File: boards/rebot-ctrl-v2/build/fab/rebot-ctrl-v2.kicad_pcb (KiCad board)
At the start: 4 copper layers, 25 x 25 mm, 57 parts, among them J1 JST-SH 8P (ESC), J2 JST-GH 4P (receiver), J3 USB-C 16P, U1 STM32G431KBU6, U2 LMR36506 buck, U3 XC6206 3.3V, U4 LSM6DSV32X, U5 W25Q128JV 16MB

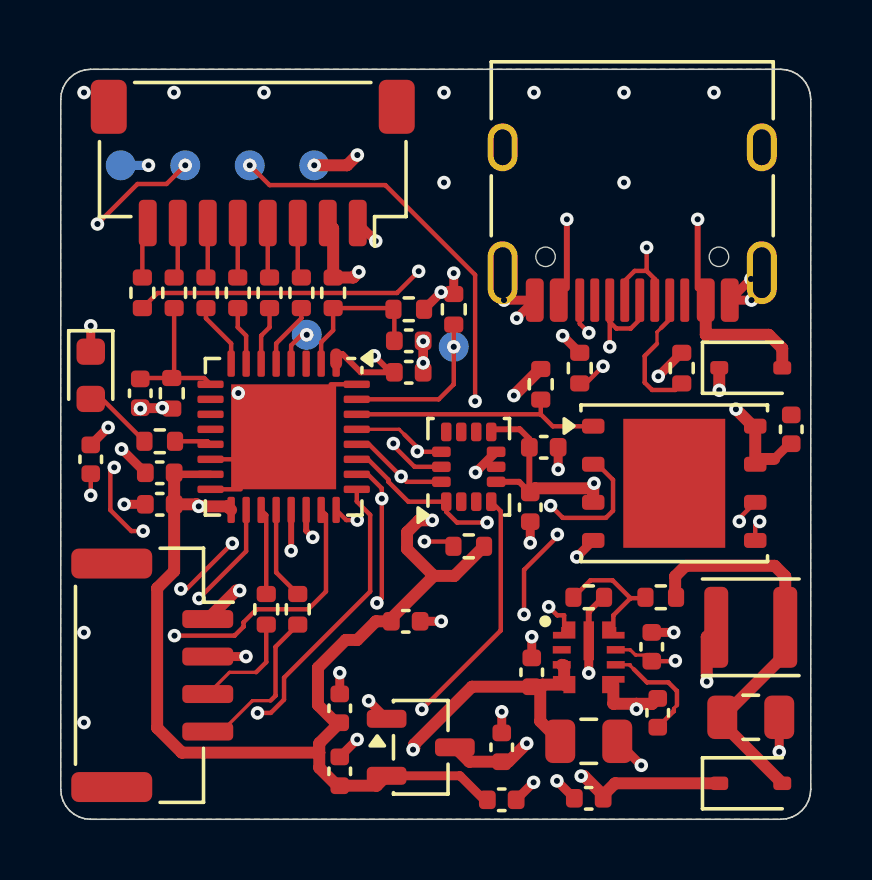
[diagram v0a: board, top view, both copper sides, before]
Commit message: rebot-ctrl-v2: JLC cost cut, 0.3/0.45 vias, Standard PCBA, GD25Q128E flash
Owner's cost cut (~$256 -> ~$188 for 5, measured on JLC's quote):
- vias 0.2/0.45 -> 0.3/0.45 (JLC's no-surcharge option; drops the Kelvin test and TG155). Board rules:
  annular ring 0.075, hole clearance 0.2 (JLC live minimum), via hole-to-hole 0.25. Rerouted, best of 8.
- lead-free HASL + green mask, Standard PCBA (the LSM6DSV32X is Standard-only; JLC adds the rails)
- U5 W25Q128JVPIQ -> GD25Q128EWIGY (pin-compatible; firmware must accept JEDEC ID C8 40 18)
- C17/C18 10 nF -> 100 nF: shares the 100 nF line, one BOM line fewer (CURR filter ~175 Hz)
- CPL: U1 -90 and J2 0 from JLC's preview

make diff: vias 102 -> 96, copper 577 -> 592 mm, SPI_SCK 6 -> 3 vias, IMU_INT1 24 -> 14 mm,
SWDIO 28 -> 39 mm, VBAT 35 -> 47 mm. Checks PASS, 0 warnings, 40 waived (new: SCK detour round the
IMU via cluster on In2, INT1 and BUCK_FB 1 mm steps). Fab set re-committed.

Co-Authored-By: Claude Opus 5.5 <noreply@anthropic.com>
Claude-Session: https://claude.ai/code/session_017ebHtPabZrHkJ3hGnLnJVi
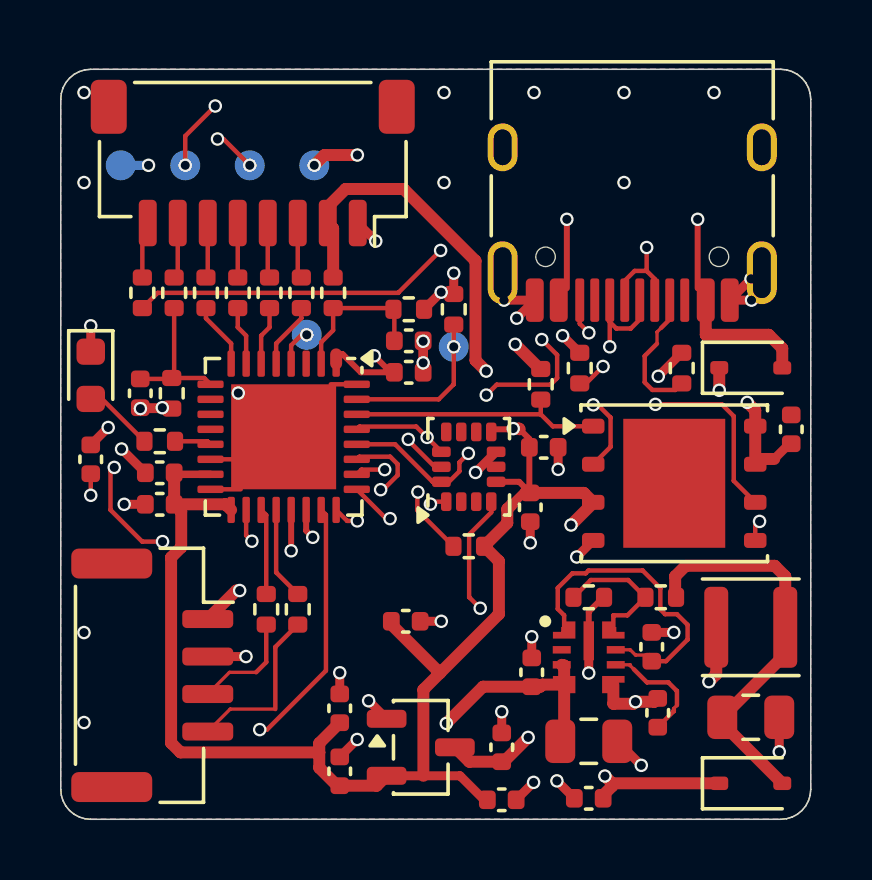
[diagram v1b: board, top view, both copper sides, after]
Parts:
- C17, C18: value 10nF -> 100nF
- U5: value W25Q128JV 16MB -> GD25Q128E 16MB
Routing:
- net VBAT: track 35.2 -> 46.8 mm
- net SWDIO: track 27.7 -> 38.9 mm, vias 5 -> 3
- net IMU_INT1: track 24.2 -> 13.8 mm
- net TLM_RX: track 38.3 -> 32.0 mm
- net 3V3: track 85.7 -> 79.5 mm, vias 8 -> 7
- net SPI_MISO: track 12.1 -> 18.0 mm, vias 2 -> 3
- net SWCLK: track 20.8 -> 26.0 mm, vias 3 -> 5
- net SPI_SCK: track 24.2 -> 21.2 mm, vias 6 -> 3
- net BUCK_VCC: track 8.32 -> 10.6 mm, vias 2 -> 0
- net SPI_MOSI: track 18.8 -> 20.9 mm
- net +5V: track 43.5 -> 45.1 mm
- net GND: vias 47 -> 46
